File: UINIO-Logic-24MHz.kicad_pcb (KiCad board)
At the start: 2 copper layers, 48.8 x 25.5 mm, 51 parts, among them J1 Conn_01x10_Pin, U1 AT24CS64-XHM, U2 74HC245C, U3 ME6211C33M5G-N, U4 CY7C68013A-56LTX, Y1 24MHz

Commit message: Release UINIO-Logic-24MHz version 3.1.0.
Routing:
- net +3.3V: track 166.4 -> 165.5 mm

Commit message: Release UINIO-Logic-24MHz version 3.1.0.
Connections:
- R25 pad 1: Net-(USB1-SBU1) -> Net-(USB1-CC2)
- USB1 pad A8: Net-(USB1-SBU1) -> unconnected-(USB1-SBU1-PadA8)
- USB1 pad B5: unconnected-(USB1-CC2-PadB5) -> Net-(USB1-CC2)
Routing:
- net Net-(USB1-SBU1): track 9.58 -> 0.00 mm, vias 2 -> 0
- net Net-(USB1-CC2): track 0.00 -> 9.08 mm, vias 0 -> 2

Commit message: Release UINIO-Logic-24MHz version 3.1.0.
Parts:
- moved J1 50.7 mm to (174.1, 94.2), turned to 0 degrees
- moved HOLE3 48.3 mm to (129.5, 115.6), turned to 180 degrees
- moved HOLE4 48.3 mm to (129.5, 95.6), turned to 180 degrees
- moved R24 41.9 mm to (132.9, 95.8), turned to 90 degrees
- moved USB1 40.8 mm to (131.0, 105.6), turned to -90 degrees
- moved D1 40.7 mm to (133.2, 114.7), turned to 90 degrees
- moved C9 39.1 mm to (134.5, 95.8), turned to 90 degrees
- moved R17 38.5 mm to (134.8, 115.2), turned to -90 degrees
- moved HOLE1 37.3 mm to (167.2, 115.6), turned to 180 degrees
- moved HOLE2 37.2 mm to (167.2, 95.6), turned to 180 degrees
- moved R25 36.4 mm to (136.0, 115.2), turned to -90 degrees
- moved R8 33.6 mm to (167.4, 100.4), turned to 0 degrees
- moved R1 33.6 mm to (167.4, 110.8), turned to 0 degrees
- moved Y1 33.5 mm to (137.1, 97.0), turned to -90 degrees
- moved R7 32.8 mm to (167.4, 101.9), turned to 0 degrees
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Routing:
- net /INPUT8: track 12.6 -> 11.8 mm
- net /INPUT7: track 14.1 -> 13.6 mm
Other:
- outline, holes or cut-outs redrawn

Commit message: Release UINIO-Logic-24MHz version 3.1.1.
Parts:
- removed ? (x2): LOGO, LOGO
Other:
- board text added: "Version 3.1.1"
- board text removed: "Version 3.1.0"

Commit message: Release UINIO-Logic-24MHz version 3.2.0.
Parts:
- moved R3 0.19 mm to (167.4, 108.0)
- moved R4 0.19 mm to (167.4, 106.5)
- moved R6 0.19 mm to (167.4, 103.6)
- moved R7 0.19 mm to (167.4, 102.1)
- moved R1 0.19 mm to (167.4, 111.0)
- moved R2 0.19 mm to (167.4, 109.5)
- moved R5 0.19 mm to (167.4, 105.1)
- moved R8 0.19 mm to (167.4, 100.6)
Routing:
- net +3.3V: track 165.5 -> 162.4 mm
- net GND: track 104.8 -> 102.0 mm, vias 23 -> 24
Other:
- board size 48.8 x 25.5 mm -> 50 x 25.5 mm
- board text added: "Version 3.2.0"
- board text removed: "Version 3.1.1"

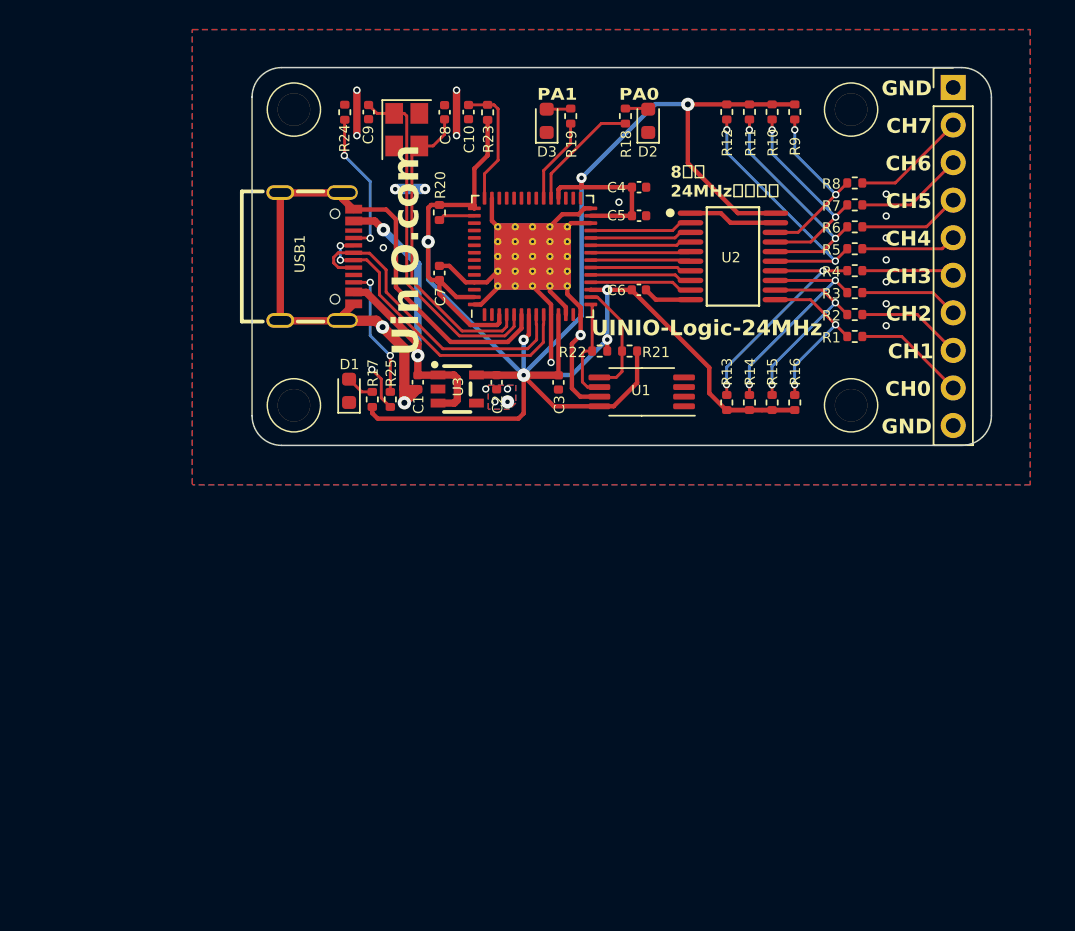
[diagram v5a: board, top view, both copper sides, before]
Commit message: Reorganize component.
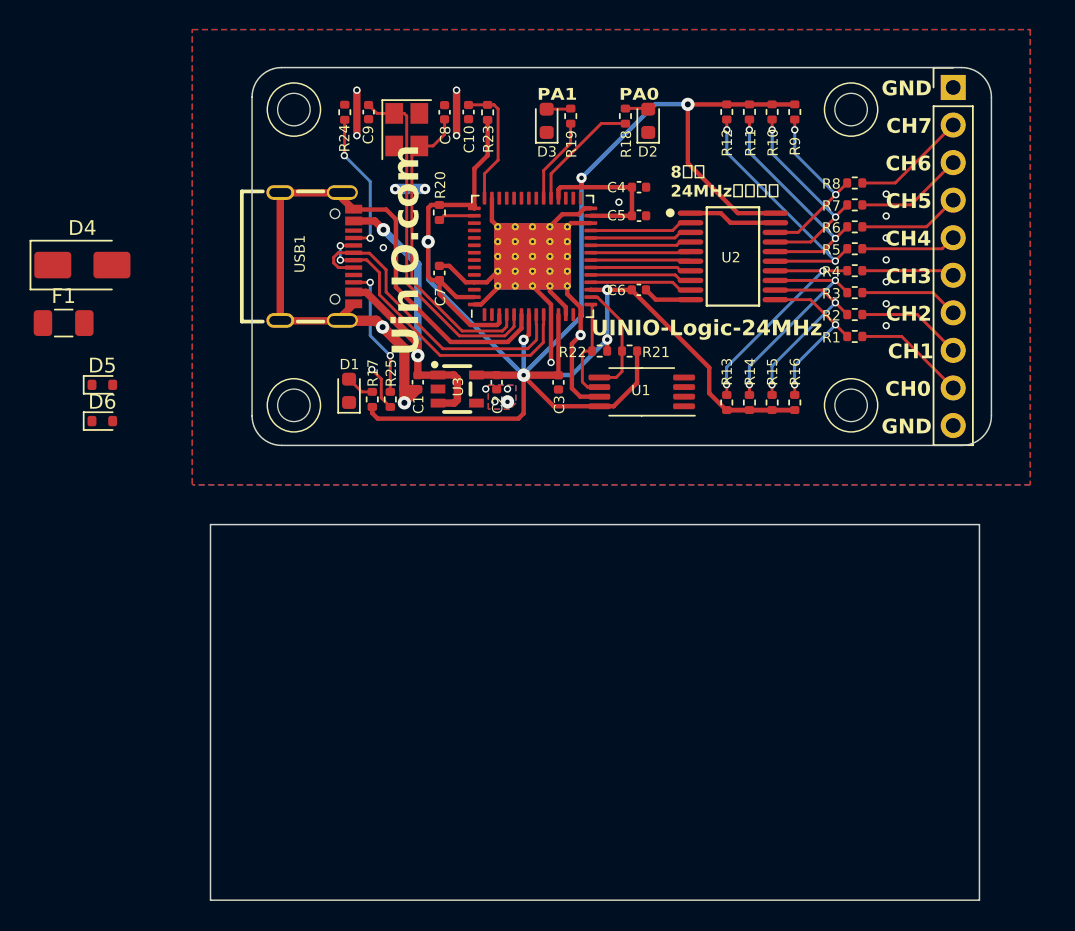
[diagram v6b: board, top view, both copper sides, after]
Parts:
- added D4: 1N4007, Diode_SMD:D_SMA, F.Cu at (115.2, 106.2)
- added D5: LESD5D5.0CT1G, Diode_SMD:D_SOD-523, F.Cu at (116.5, 114.3)
- added D6: LESD5D5.0CT1G, Diode_SMD:D_SOD-523, F.Cu at (116.5, 116.7)
- added F1: 60V 1A, Fuse:Fuse_1206_3216Metric, F.Cu at (113.9, 110.1)
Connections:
- C2 pad 2: +3.3V -> Net-(U3-Vout)
- R17 pad 2: +3.3V -> Net-(U3-Vout)
- U3 pad 5: +3.3V -> Net-(U3-Vout)
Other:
- board size 50 x 25.5 mm -> 52.8 x 56.3 mm

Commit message: Reorganize component.
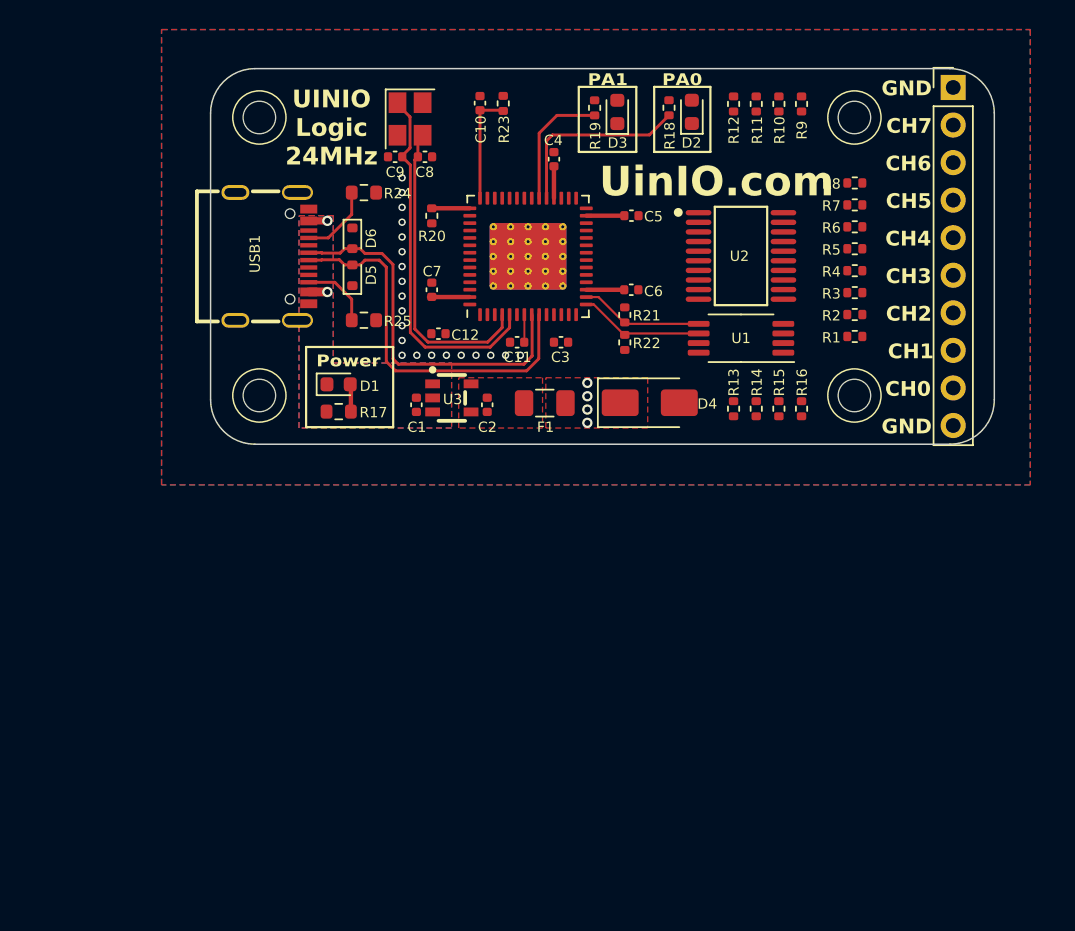
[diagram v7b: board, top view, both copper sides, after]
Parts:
- added C11: 0.1uF, Capacitor_SMD:C_0402_1005Metric, F.Cu at (144.6, 111.4)
- added C12: 0.1uF, Capacitor_SMD:C_0402_1005Metric, F.Cu at (139.2, 110.8)
- R17, R24, R25: footprint Resistor_SMD:R_0402_1005Metric -> Resistor_SMD:R_0603_1608Metric
- moved D4 39.5 mm to (153.5, 115.5)
- moved F1 33.0 mm to (146.4, 115.5), turned to 180 degrees
- moved D6 20.9 mm to (133.4, 104.3), turned to -90 degrees
- moved D5 18.5 mm to (133.4, 106.8), turned to 90 degrees
- moved U1 7.63 mm to (159.7, 111.1)
- moved C4 6.06 mm to (147.1, 99.0), turned to 90 degrees
- moved R25 5.64 mm to (134.2, 109.9), turned to 0 degrees
- moved R24 5.59 mm to (134.2, 101.3), turned to 0 degrees
- moved D3 4.81 mm to (151.3, 95.8)
- moved C9 3.52 mm to (136.3, 98.8), turned to 0 degrees
- moved C8 3.29 mm to (138.3, 98.8), turned to 180 degrees
- moved USB1 3.04 mm to (128.0, 105.6)
- moved D2 3.01 mm to (156.4, 95.8)
- moved R18 3.00 mm to (154.8, 95.5)
- moved C3 2.72 mm to (147.5, 111.4), turned to 0 degrees
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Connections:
- F1 pad 1: +3.3V -> Net-(U3-Vout)
- F1 pad 2: Net-(U3-Vout) -> +3.3V
- R17 pad 2: Net-(U3-Vout) -> +3.3V
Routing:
- net +3.3V: track 162.4 -> 14.5 mm, vias 7 -> 4
- net GND: track 102.0 -> 0.00 mm, vias 24 -> 21
- net +5V: track 25.2 -> 2.53 mm
- net /INPUT4: track 17.8 -> 0.00 mm, vias 2 -> 0
- net /INPUT3: track 16.0 -> 0.00 mm, vias 2 -> 0
- net /INPUT5: track 16.0 -> 0.00 mm, vias 2 -> 0
- net /INPUT6: track 15.3 -> 0.00 mm, vias 2 -> 0
- net /INPUT2: track 14.3 -> 0.00 mm, vias 2 -> 0
- net /INPUT7: track 13.6 -> 0.00 mm, vias 2 -> 0
- net /INPUT1: track 12.5 -> 0.00 mm, vias 2 -> 0
- net /INPUT8: track 11.8 -> 0.00 mm, vias 2 -> 0
- net Net-(J1-Pin_2): track 7.77 -> 0.00 mm
- net Net-(J1-Pin_9): track 7.59 -> 0.00 mm
- net Net-(J1-Pin_3): track 7.33 -> 0.00 mm
- net Net-(J1-Pin_8): track 7.15 -> 0.00 mm
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- added copper zone on F.Cu, net +3.3V
- added copper zone on B.Cu, net +5V
- added copper zone on F.Cu, net +5V
- added copper zone on F.Cu, net Net-(U3-Vout)
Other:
- board size 52.8 x 56.3 mm -> 53 x 25.4 mm
- board text added: "Power"
- board text added: "UINIO Logic 24MHz"
- board text added: "Version 5.0.0"
- board text removed: "8通道 24MHz采样频率"
- board text removed: "Version 3.2.0"
